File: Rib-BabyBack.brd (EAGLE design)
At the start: 67.3 x 74.9 mm, 23 parts, among them IC1 REG1117, SW1 DPDT

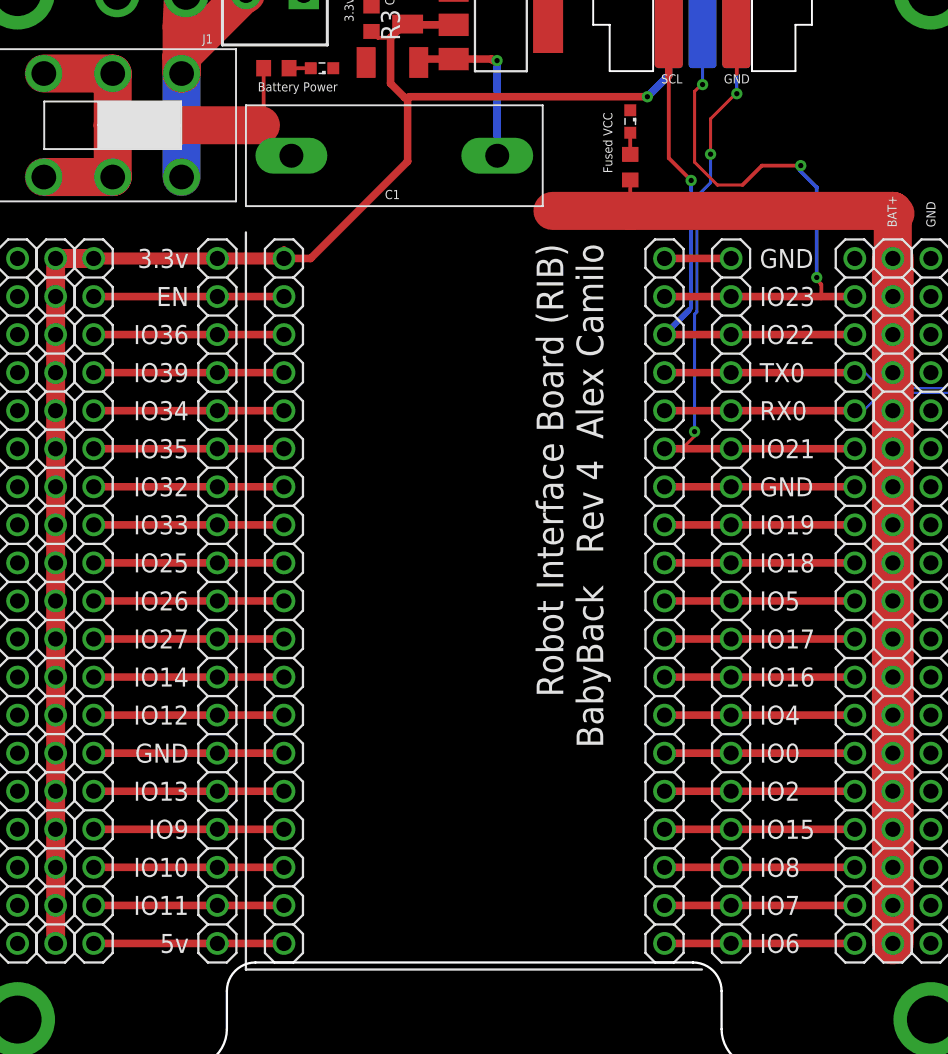
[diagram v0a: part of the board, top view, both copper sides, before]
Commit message: Issue #26 Disconnect specific IO used by System Resources on ESP32
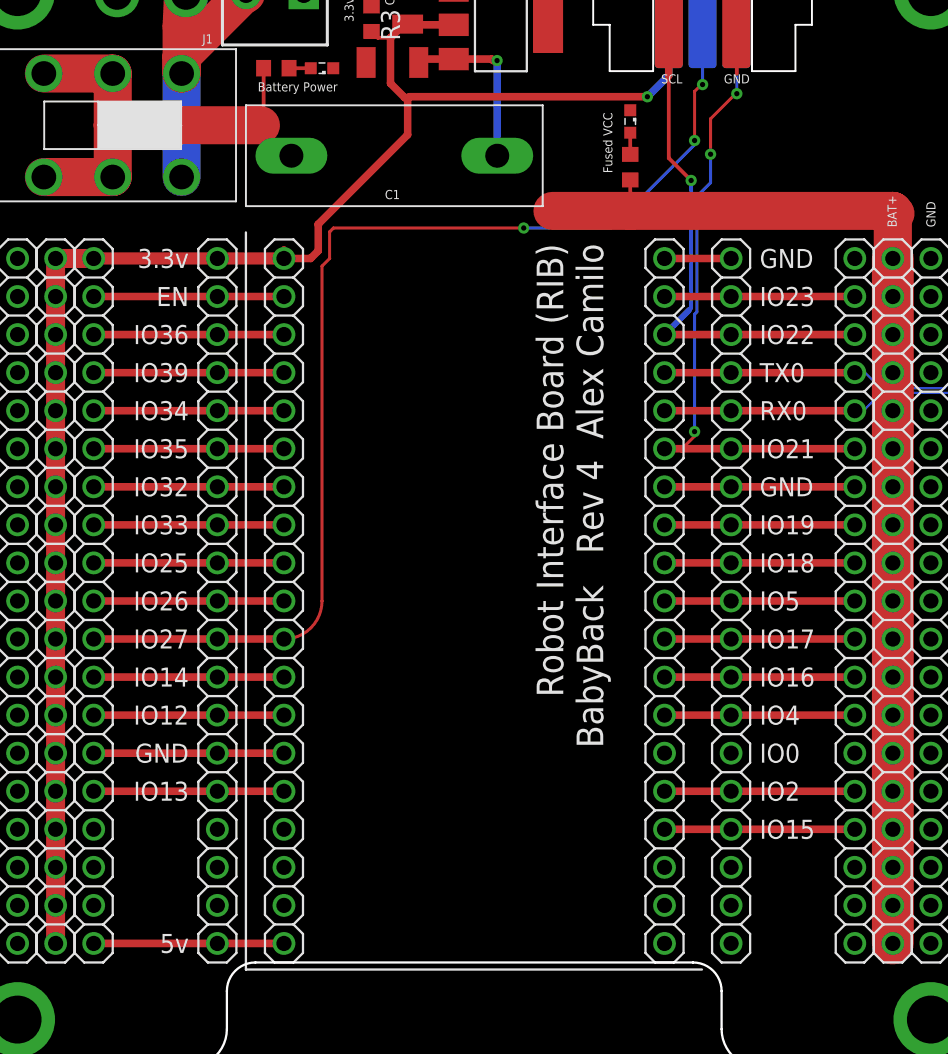
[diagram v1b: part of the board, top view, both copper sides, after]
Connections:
- removed net N$14: JP2.9, JP3.9, JP6.9
- removed net N$25: JP17.1, JP7.1, JP8.1
- removed net N$26: JP17.2, JP7.2, JP8.2
- removed net N$27: JP17.3, JP7.3, JP8.3
- removed net N$30: JP17.6, JP7.6, JP8.6
- removed net N$7: JP2.2, JP3.2, JP6.2
- removed net N$8: JP2.3, JP3.3, JP6.3
- removed net N$9: JP2.4, JP3.4, JP6.4
- new net P18: JP17.18, JP7.18, JP8.18
- net DET: now also JP2.9, JP3.9, JP6.9; no longer JP17.18, JP7.18, JP8.18
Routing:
- net DET: track 37.2 -> 73.4 mm
- net N$9: track 12.7 -> 0.00 mm
- net N$8: track 12.7 -> 0.00 mm
- net N$7: track 12.7 -> 0.00 mm
- net N$14: track 12.7 -> 0.00 mm
- net P18: track 0.00 -> 12.7 mm
- net N$30: track 12.7 -> 0.00 mm
- net N$27: track 12.7 -> 0.00 mm
- net N$26: track 12.7 -> 0.00 mm
- net N$25: track 12.7 -> 0.00 mm
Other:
- board text removed: "IO10"
- board text removed: "IO11"
- board text removed: "IO6"
- board text removed: "IO7"
- board text removed: "IO8"
- board text removed: "IO9"
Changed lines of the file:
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@@
 <text x="-3.81" y="17.145" size="1.27" layer="21" font="vector" ratio="20" align="bottom-right">GND</text>
 <text x="-3.81" y="14.605" size="1.27" layer="21" font="vector" ratio="20" align="bottom-right">IO13</text>
-<text x="-3.81" y="12.065" size="1.27" layer="21" font="vector" ratio="20" align="bottom-right">IO9</text>
-<text x="-3.81" y="9.525" size="1.27" layer="21" font="vector" ratio="20" align="bottom-right">IO10</text>
-<text x="-3.81" y="6.985" size="1.27" layer="21" font="vector" ratio="20" align="bottom-right">IO11</text>
 <text x="-3.81" y="4.445" size="1.27" layer="21" font="vector" ratio="20" align="bottom-right">5v</text>
 <text x="34.29" y="50.165" size="1.27" layer="21" font="vector" ratio="20">GND</text>
@@
 <text x="34.29" y="14.605" size="1.27" layer="21" font="vector" ratio="20">IO2</text>
 <text x="34.29" y="12.065" size="1.27" layer="21" font="vector" ratio="20">IO15</text>
-<text x="34.29" y="9.525" size="1.27" layer="21" font="vector" ratio="20">IO8</text>
-<text x="34.29" y="6.985" size="1.27" layer="21" font="vector" ratio="20">IO7</text>
-<text x="34.29" y="4.445" size="1.27" layer="21" font="vector" ratio="20">IO6</text>
 <wire x1="30.48" y1="3.34" x2="0.04" y2="3.34" width="0.1524" layer="22"/>
 <wire x1="30.48" y1="3.34" x2="30.48" y2="52.54" width="0.1524" layer="22"/>
@@
 <contactref element="LED1" pad="C"/>
 </signal>
-<signal name="N$7">
-<contactref element="JP2" pad="2"/>
-<contactref element="JP3" pad="2"/>
-<contactref element="JP6" pad="2"/>
-<wire x1="2.54" y1="7.62" x2="-1.905" y2="7.62" width="0.508" layer="1"/>
-<wire x1="-1.905" y1="7.62" x2="-10.16" y2="7.62" width="0.508" layer="1"/>
-</signal>
-<signal name="N$8">
-<contactref element="JP2" pad="3"/>
-<contactref element="JP3" pad="3"/>
-<contactref element="JP6" pad="3"/>
-<wire x1="-10.16" y1="10.16" x2="-1.905" y2="10.16" width="0.508" layer="1"/>
-<wire x1="-1.905" y1="10.16" x2="2.54" y2="10.16" width="0.508" layer="1"/>
-</signal>
-<signal name="N$9">
-<contactref element="JP2" pad="4"/>
-<contactref element="JP3" pad="4"/>
-<contactref element="JP6" pad="4"/>
-<wire x1="2.54" y1="12.7" x2="-1.905" y2="12.7" width="0.508" layer="1"/>
-<wire x1="-1.905" y1="12.7" x2="-10.16" y2="12.7" width="0.508" layer="1"/>
-</signal>
 <signal name="N$10">
 <contactref element="JP2" pad="5"/>
@@
 <wire x1="-1.905" y1="22.86" x2="-10.16" y2="22.86" width="0.508" layer="1"/>
 </signal>
-<signal name="N$14">
-<contactref element="JP2" pad="9"/>
-<contactref element="JP3" pad="9"/>
-<contactref element="JP6" pad="9"/>
-<wire x1="-10.16" y1="25.4" x2="-1.905" y2="25.4" width="0.508" layer="1"/>
-<wire x1="-1.905" y1="25.4" x2="2.54" y2="25.4" width="0.508" layer="1"/>
-</signal>
 <signal name="N$15">
 <contactref element="JP2" pad="10"/>
@@
 <wire x1="-1.905" y1="48.26" x2="-10.16" y2="48.26" width="0.508" layer="1"/>
 </signal>
-<signal name="N$25">
-<contactref element="JP8" pad="1"/>
-<contactref element="JP17" pad="1"/>
-<contactref element="JP7" pad="1"/>
-<wire x1="27.94" y1="5.08" x2="32.385" y2="5.08" width="0.508" layer="1"/>
-<wire x1="32.385" y1="5.08" x2="40.64" y2="5.08" width="0.508" layer="1"/>
-</signal>
-<signal name="N$26">
-<contactref element="JP8" pad="2"/>
-<contactref element="JP17" pad="2"/>
-<contactref element="JP7" pad="2"/>
-<wire x1="40.64" y1="7.62" x2="32.385" y2="7.62" width="0.508" layer="1"/>
-<wire x1="32.385" y1="7.62" x2="27.94" y2="7.62" width="0.508" layer="1"/>
-</signal>
-<signal name="N$27">
-<contactref element="JP8" pad="3"/>
-<contactref element="JP17" pad="3"/>
-<contactref element="JP7" pad="3"/>
-<wire x1="27.94" y1="10.16" x2="32.385" y2="10.16" width="0.508" layer="1"/>
-<wire x1="32.385" y1="10.16" x2="40.64" y2="10.16" width="0.508" layer="1"/>
-</signal>
 <signal name="N$28">
 <contactref element="JP8" pad="4"/>
@@
 <wire x1="27.94" y1="15.24" x2="32.385" y2="15.24" width="0.508" layer="1"/>
 <wire x1="32.385" y1="15.24" x2="40.64" y2="15.24" width="0.508" layer="1"/>
-</signal>
-<signal name="N$30">
-<contactref element="JP8" pad="6"/>
-<contactref element="JP17" pad="6"/>
-<contactref element="JP7" pad="6"/>
-<wire x1="40.64" y1="17.78" x2="32.385" y2="17.78" width="0.508" layer="1"/>
-<wire x1="32.385" y1="17.78" x2="27.94" y2="17.78" width="0.508" layer="1"/>
 </signal>
 <signal name="N$31">
@@
 <wire x1="-1.905" y1="50.8" x2="-10.16" y2="50.8" width="0.8128" layer="1"/>
 <wire x1="2.54" y1="50.8" x2="-1.905" y2="50.8" width="0.8128" layer="1"/>
-<wire x1="10.795" y1="57.277" x2="10.795" y2="61.468" width="0.508" layer="1"/>
-<wire x1="4.318" y1="50.8" x2="10.795" y2="57.277" width="0.508" layer="1"/>
 <wire x1="13.8684" y1="66.3956" x2="10.8434" y2="66.3956" width="0.508" layer="1"/>
 <wire x1="10.8434" y1="66.3956" x2="10.795" y2="66.444" width="0.508" layer="1"/>
@@
 <wire x1="8.382" y1="65.952" x2="8.802" y2="65.532" width="0.254" layer="1"/>
 <wire x1="8.802" y1="65.532" x2="9.652" y2="65.532" width="0.254" layer="1"/>
+<wire x1="4.318" y1="50.8" x2="4.826" y2="51.308" width="0.508" layer="1"/>
+<wire x1="4.826" y1="51.308" x2="4.826" y2="53.086" width="0.508" layer="1"/>
+<wire x1="4.826" y1="53.086" x2="10.795" y2="59.055" width="0.508" layer="1"/>
+<wire x1="10.795" y1="59.055" x2="10.795" y2="61.468" width="0.508" layer="1"/>
 <wire x1="-12.7" y1="45.72" x2="-12.7" y2="48.26" width="0" layer="19" extent="1-1"/>
 <wire x1="-12.7" y1="43.18" x2="-12.7" y2="45.72" width="0" layer="19" extent="1-1"/>
@@
 </signal>
 <signal name="DET">
-<contactref element="JP17" pad="18"/>
-<contactref element="JP8" pad="18"/>
-<contactref element="JP7" pad="18"/>
-<wire x1="27.94" y1="48.26" x2="32.385" y2="48.26" width="0.508" layer="1"/>
-<wire x1="32.385" y1="48.26" x2="38.4048" y2="48.26" width="0.508" layer="1"/>
 <contactref element="U$5" pad="ATT"/>
-<wire x1="38.4048" y1="48.26" x2="40.64" y2="48.26" width="0.508" layer="1"/>
-<wire x1="38.4048" y1="48.26" x2="38.4048" y2="49.0728" width="0.254" layer="1"/>
-<wire x1="38.4048" y1="49.0728" x2="37.9476" y2="49.53" width="0.254" layer="1"/>
-<wire x1="37.9476" y1="49.53" x2="38.1" y2="49.53" width="0.254" layer="1"/>
-<via x="38.1" y="49.53" extent="1-16" drill="0.35"/>
-<wire x1="38.1" y1="49.53" x2="38.1" y2="55.5498" width="0.254" layer="16"/>
-<wire x1="38.1" y1="55.5498" x2="36.957" y2="56.6928" width="0.254" layer="16"/>
-<wire x1="36.957" y1="56.6928" x2="37.0332" y2="56.769" width="0.254" layer="16"/>
-<wire x1="37.0332" y1="56.769" x2="37.0332" y2="56.9976" width="0.254" layer="16"/>
-<via x="37.0332" y="56.9976" extent="1-16" drill="0.35"/>
-<wire x1="37.0332" y1="56.9976" x2="34.4424" y2="56.9976" width="0.254" layer="1"/>
-<wire x1="34.4424" y1="56.9976" x2="33.147" y2="55.7022" width="0.254" layer="1"/>
-<wire x1="33.147" y1="55.7022" x2="31.4706" y2="55.7022" width="0.2032" layer="1"/>
-<wire x1="31.4706" y1="55.7022" x2="29.9466" y2="57.2262" width="0.2032" layer="1"/>
-<wire x1="29.9466" y1="57.2262" x2="29.9466" y2="61.9506" width="0.2032" layer="1"/>
+<wire x1="29.9466" y1="58.674" x2="29.9466" y2="61.9506" width="0.2032" layer="1"/>
 <wire x1="29.9466" y1="61.9506" x2="30.4038" y2="62.4078" width="0.2032" layer="1"/>
 <wire x1="30.4038" y1="62.4078" x2="30.48" y2="62.4078" width="0.2032" layer="1"/>
@@
 <wire x1="30.48" y1="62.4078" x2="30.48" y2="63.5508" width="0.2032" layer="16"/>
 <wire x1="30.48" y1="63.5508" x2="30.4038" y2="63.627" width="0.2032" layer="16"/>
+<contactref element="JP2" pad="9"/>
+<contactref element="JP3" pad="9"/>
+<contactref element="JP6" pad="9"/>
+<wire x1="-10.16" y1="25.4" x2="-1.905" y2="25.4" width="0.508" layer="1"/>
+<wire x1="-1.905" y1="25.4" x2="2.54" y2="25.4" width="0.508" layer="1"/>
+<wire x1="2.54" y1="25.4" x2="5.08" y2="27.94" width="0.2032" layer="1" curve="90"/>
+<wire x1="5.08" y1="27.94" x2="5.08" y2="50.292" width="0.2032" layer="1"/>
+<wire x1="5.08" y1="50.292" x2="5.588" y2="50.8" width="0.2032" layer="1"/>
+<wire x1="5.588" y1="50.8" x2="5.588" y2="52.578" width="0.2032" layer="1"/>
+<wire x1="5.588" y1="52.578" x2="5.842" y2="52.832" width="0.2032" layer="1"/>
+<via x="18.542" y="52.832" extent="1-16" drill="0.35"/>
+<wire x1="18.542" y1="52.832" x2="24.384" y2="52.832" width="0.2032" layer="16"/>
+<wire x1="29.9466" y1="58.3946" x2="29.9466" y2="58.674" width="0.2032" layer="16"/>
+<via x="29.9466" y="58.674" extent="1-16" drill="0.35"/>
+<wire x1="5.842" y1="52.832" x2="18.542" y2="52.832" width="0.2032" layer="1"/>
+<wire x1="24.384" y1="52.832" x2="29.9466" y2="58.3946" width="0.2032" layer="16"/>
 <wire x1="30.4038" y1="63.627" x2="30.48" y2="67.505" width="0" layer="19" extent="16-16"/>
 </signal>
@@
 <wire x1="8.382" y1="67.652" x2="8.382" y2="69.1" width="0.254" layer="1"/>
 </signal>
+<signal name="P18">
+<contactref element="JP17" pad="18"/>
+<contactref element="JP8" pad="18"/>
+<contactref element="JP7" pad="18"/>
+<wire x1="27.94" y1="48.26" x2="32.385" y2="48.26" width="0.508" layer="1"/>
+<wire x1="32.385" y1="48.26" x2="40.64" y2="48.26" width="0.508" layer="1"/>
+</signal>
 </signals>

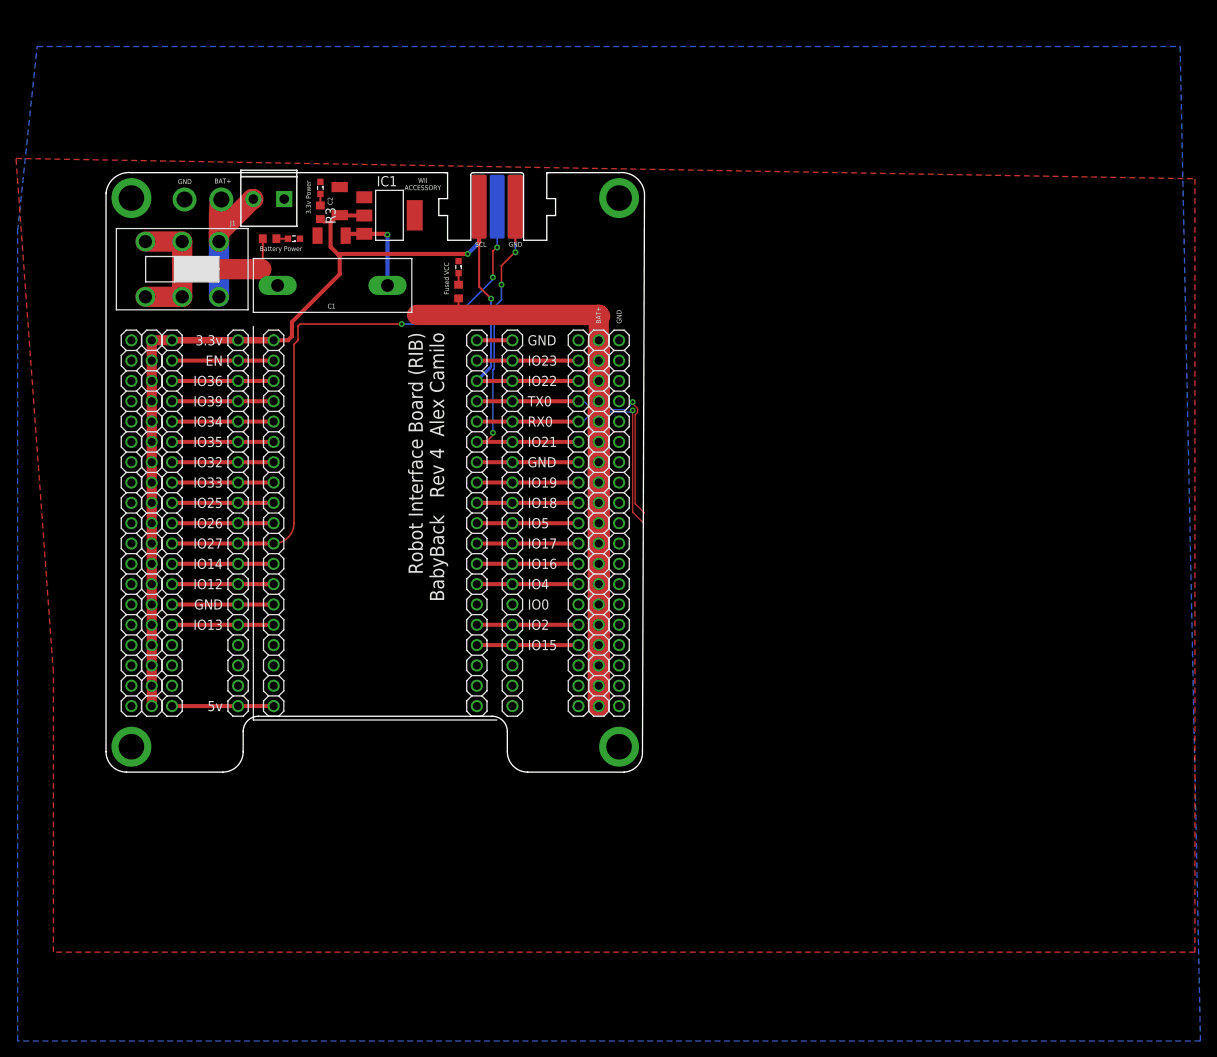
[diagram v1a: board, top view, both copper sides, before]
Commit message: Issue #32 ESP32 needs a user accessible LED on 13
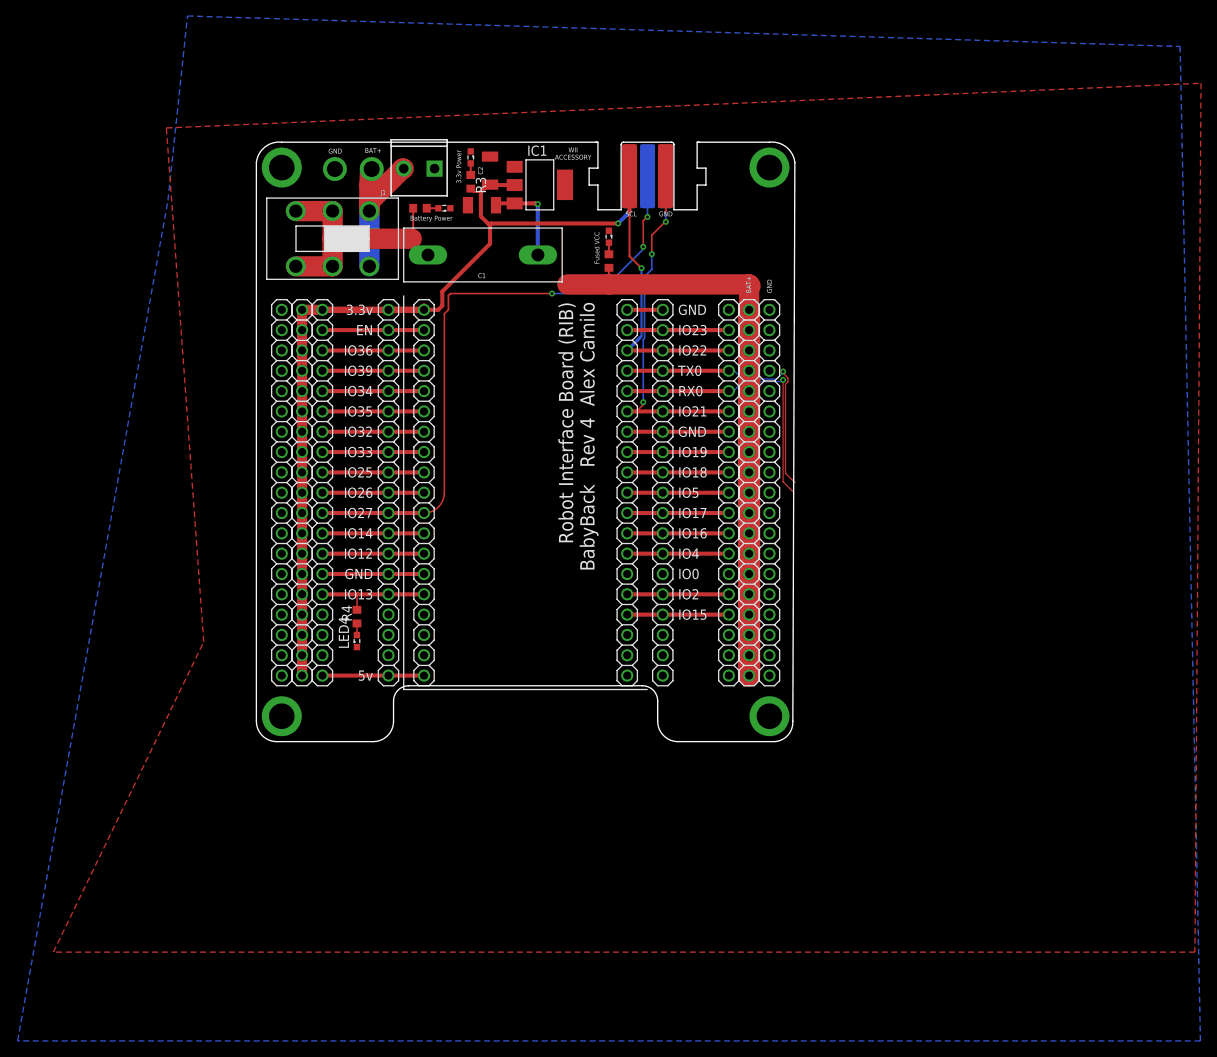
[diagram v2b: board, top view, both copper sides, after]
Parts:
- added LED4: (no value), eagle-ltspice:LED_SML0603
- added R4: (no value), resistor:R0603
- moved JP19 19.2 mm to (64.5, 31.8)
- moved LED1 19.2 mm to (44.5, 63.8)
- moved R1 19.2 mm to (44.5, 60.7)
- moved U$5 19.2 mm to (49.3, 75.6)
- moved C1 19.2 mm to (28.6, 67.7)
- moved C2 19.2 mm to (29.6, 72.0)
- moved F4 19.2 mm to (28.7, 61.5)
- moved J1 19.2 mm to (22.5, 72.3)
- moved JP17 19.2 mm to (59.4, 31.8)
- moved JP18 19.2 mm to (62.0, 31.8)
- moved JP2 19.2 mm to (16.9, 31.8)
- moved JP3 19.2 mm to (8.64, 31.8)
- moved JP4 19.2 mm to (6.10, 31.8)
- moved JP5 19.2 mm to (3.56, 31.8)
- moved JP6 19.2 mm to (21.3, 31.8)
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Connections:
- removed net N$10: JP2.5, JP3.5, JP6.5
- new net N$1: LED4.A, R4.1
- new net P13: JP2.5, JP3.5, JP6.5, R4.2
- net GND: now also LED4.C
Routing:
- net P13: track 0.00 -> 14.6 mm
- net N$10: track 12.7 -> 0.00 mm
- net N$1: track 0.00 -> 1.45 mm
